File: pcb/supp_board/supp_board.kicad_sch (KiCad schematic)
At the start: 19 parts, among them J1 Conn_01x03_Pin, J2 Conn_01x02_Pin, J3 Screw_Terminal_01x04, J4 Screw_Terminal_01x04, J5 Screw_Terminal_01x04, J6 Conn_01x08_Socket, J7 Conn_01x08_Socket, J8 Conn_01x08_Socket, J9 Conn_01x08_Socket, Q1 IRLZ44N, Q2 IRLZ44N, Q3 IRLZ44N, Q7 IRLZ44N, Q8 IRLZ44N, Q9 IRLZ44N

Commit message: Add work from 2025-07-24 to 2025-07-26
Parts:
- removed J1: Conn_01x03_Pin, Connector_Wire:SolderWire-0.5sqmm_1x03_P4.6mm_D0.9mm_OD2.1mm, symbol Connector:Conn_01x03_Pin
- added C1, C2, C3: C_Polarized, Capacitor_THT:CP_Radial_D8.0mm_P3.50mm, symbol Device:C_Polarized
- added J10: Screw_Terminal_01x03, TerminalBlock:TerminalBlock_MaiXu_MX126-5.0-03P_1x03_P5.00mm, symbol Connector:Screw_Terminal_01x03
- J6, J7, J8, J9: footprint Connector_JST:JST_PH_S8B-PH-K_1x08_P2.00mm_Horizontal -> Connector_JST:JST_PH_B8B-PH-K_1x08_P2.00mm_Vertical
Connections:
- net TX: now reaches A2.1 (GPIO0), J2.2 (Pin_2)
- net GND: now reaches A1.1 (GND), A1.7 (GND), A2.13 (GND), A2.18 (GND), A2.23 (GND), A2.28 (GND), A2.3 (GND), A2.38 (GND), A2.8 (GND), A3.1 (GND), A3.7 (GND), A4.1 (GND), A4.7 (GND), J6.4 (Pin_4), J7.4 (Pin_4), J8.4 (Pin_4)
- net GND: now also C1.2, C2.2, C3.2, J10.2 (Pin_2); no longer J9.2 (Pin_2)
- net RX: now reaches A2.2 (GPIO1), J2.1 (Pin_1)
- net +5V: now reaches A1.10 (M0), A1.11 (M1), A1.12 (M2), A1.13 (~{RST}), A1.14 (~{SLP}), A2.40 (VBUS), A4.10 (M0), A4.11 (M1), A4.12 (M2), A4.13 (~{RST}), A4.14 (~{SLP}), Q7.3 (S), Q8.3 (S), Q9.3 (S)
- net +5V: now also A3.10 (M0), A3.11 (M1), A3.12 (M2), A3.13 (~{RST}), A3.14 (~{SLP}), J10.1 (Pin_1)
- net TPLG_TX: now reaches A2.6 (GPIO4), J6.5 (Pin_5)
- net TPLG_RX: now reaches A2.7 (GPIO5), J6.6 (Pin_6)
- net +24V: now reaches Q1.3 (S), Q2.3 (S), Q3.3 (S)
- net +24V: now also A1.8 (VMOT), A3.8 (VMOT), A4.8 (VMOT), C1.1, C2.1, C3.1, J10.3 (Pin_3)
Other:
- note added: "place @ drv 1"
- note added: "place @ drv 2"
- note added: "place @ drv 3"

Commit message: Add work from 2025-07-27
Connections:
- net GND: now also J9.2 (Pin_2)
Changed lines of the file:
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@@
+	)
+	(symbol
+		(lib_id "power:GND")
+		(at 162.56 123.19 0)
+		(mirror x)
+		(unit 1)
+		(exclude_from_sim no)
+		(in_bom yes)
+		(on_board yes)
+		(dnp no)
+		(property "Reference" "#PWR012"
+			(at 162.56 116.84 0)
+			(effects
+				(font
+					(size 1.27 1.27)
+				)
+				(hide yes)
+			)
+		)
+		(property "Value" "GND"
+			(at 162.56 118.11 0)
+			(effects
+				(font
+					(size 1.27 1.27)
+				)
+			)
+		)
+		(property "Footprint" ""
+			(at 162.56 123.19 0)
+			(effects
+				(font
+					(size 1.27 1.27)
+				)
+				(hide yes)
+			)
+		)
+		(property "Datasheet" ""
+			(at 162.56 123.19 0)
+			(effects
+				(font
+					(size 1.27 1.27)
+				)
+				(hide yes)
+			)
+		)
+		(property "Description" "Power symbol creates a global label with name \"GND\" , ground"
+			(at 162.56 123.19 0)
+			(effects
+				(font
+					(size 1.27 1.27)
+				)
+				(hide yes)
+			)
+		)
+		(pin "1"
+		)
+		(instances
+			(project ""
+				(path "/21a5de1d-7745-4c12-9064-9c9b9fdd4bd4"
+					(reference "#PWR012")
+					(unit 1)
+				)
+			)
+		)
 	)
 	(symbol

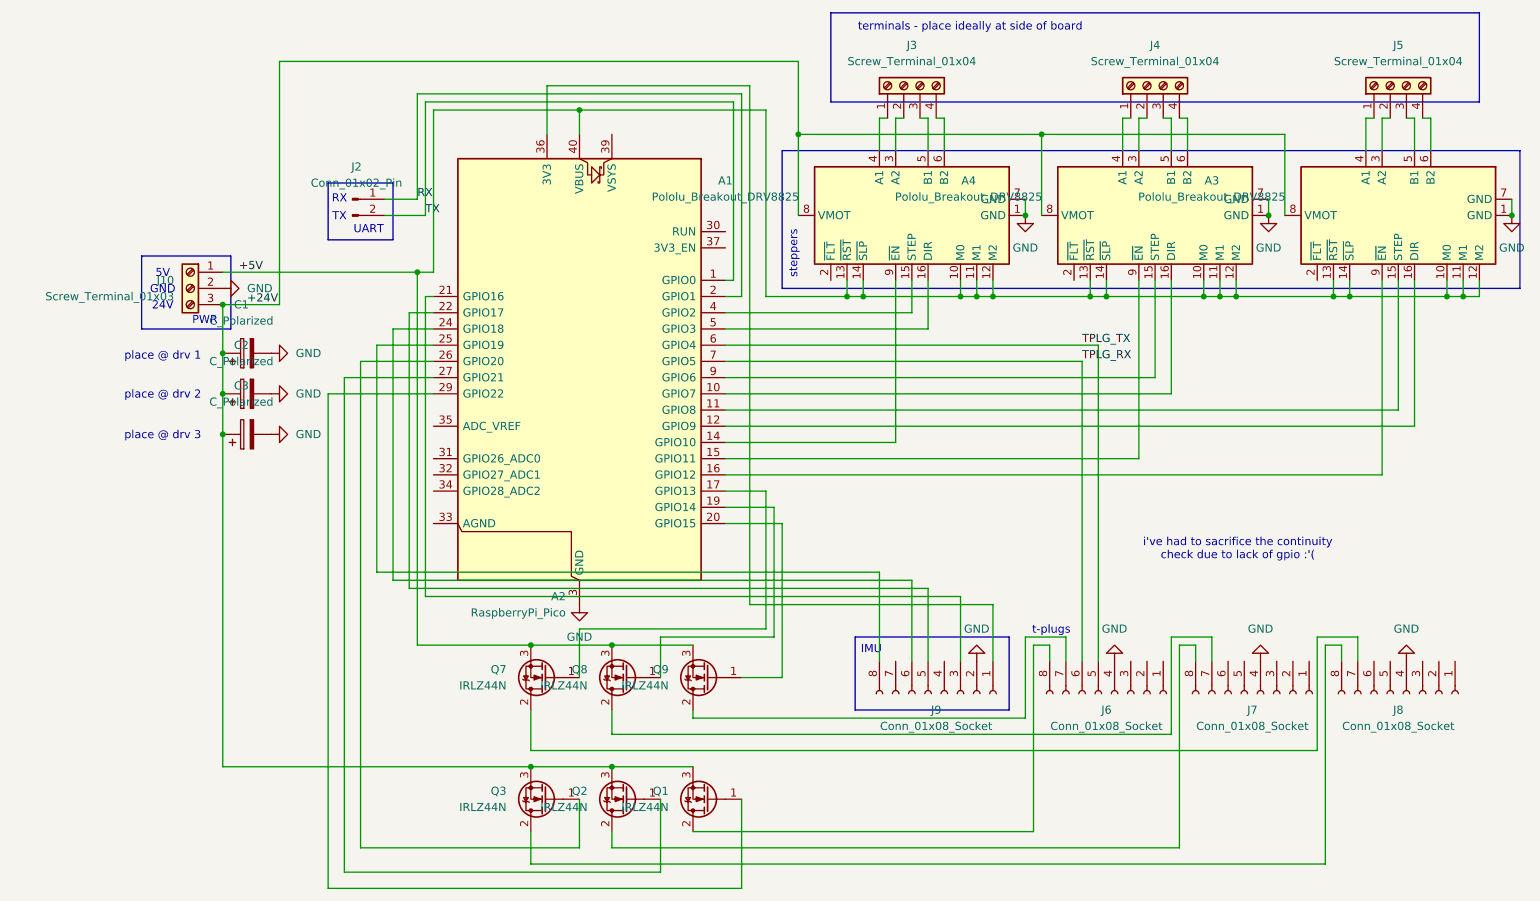
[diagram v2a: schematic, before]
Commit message: Reroute supp. board
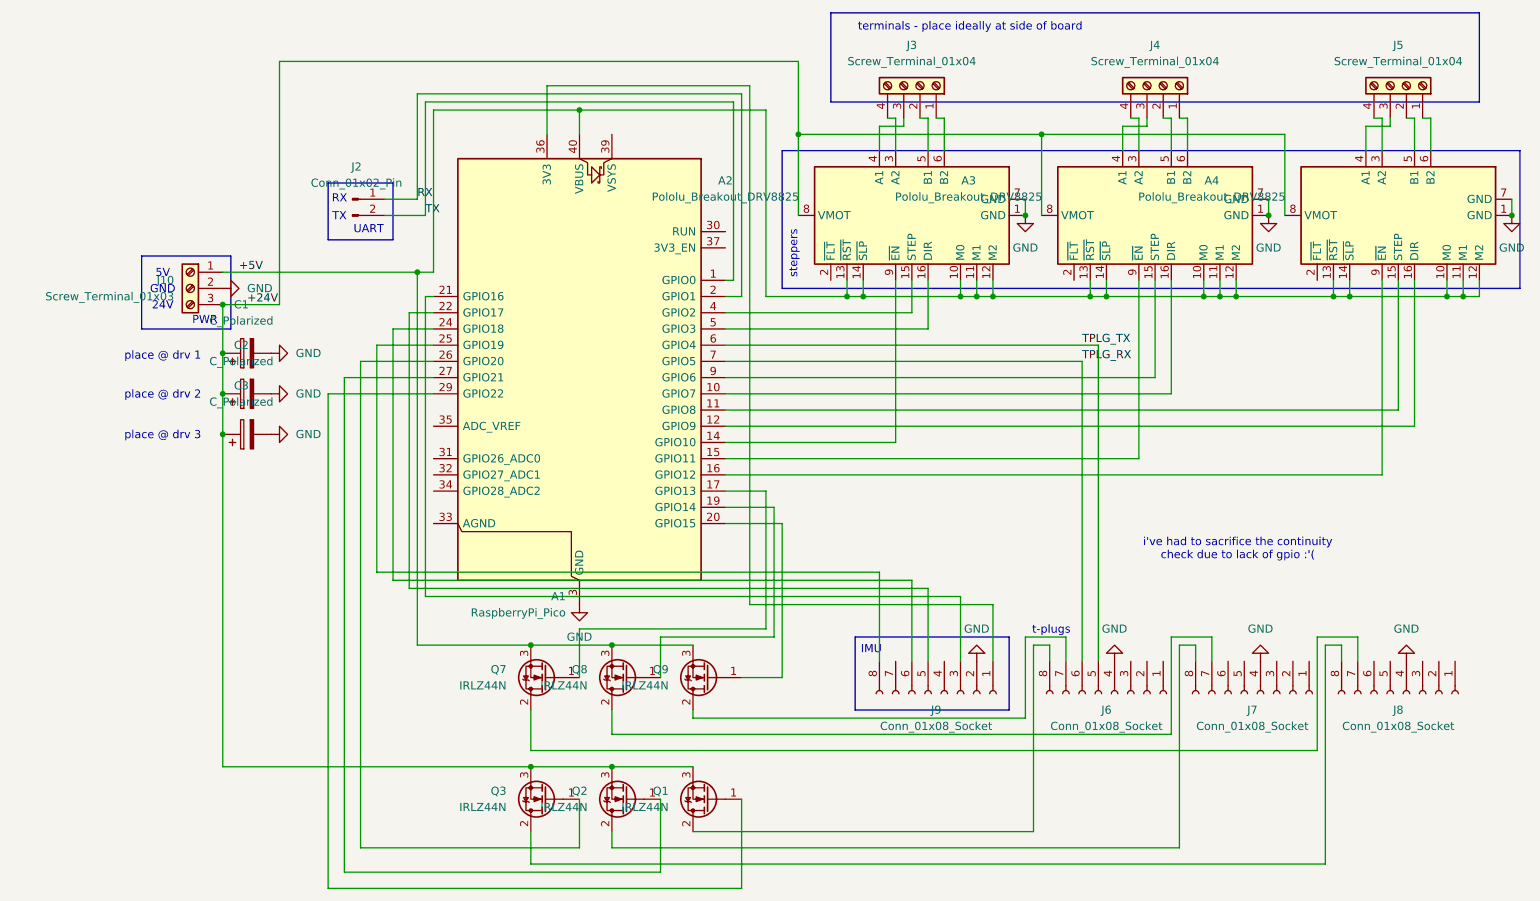
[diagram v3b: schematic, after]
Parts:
- renumbered A2 to A1, A1 to A2, A4 to A3, A3 to A4
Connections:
- net at J4.1 (Pin_1): now also A3.6 (B2); no longer A3.4 (A1)
- net at J4.2 (Pin_2): now also A3.5 (B1); no longer A3.3 (A2)
- net at J4.3 (Pin_3): now also A3.4 (A1); no longer A3.5 (B1)
- net at J4.4 (Pin_4): now also A3.3 (A2); no longer A3.6 (B2)
- net at A2.3 (A2): now also J3.4 (Pin_4); no longer J3.2 (Pin_2)
- net at A2.4 (A1): now also J3.3 (Pin_3); no longer J3.1 (Pin_1)
- net at A2.5 (B1): now also J3.2 (Pin_2); no longer J3.3 (Pin_3)
- net at A2.6 (B2): now also J3.1 (Pin_1); no longer J3.4 (Pin_4)
- net at J5.1 (Pin_1): now also A4.6 (B2); no longer A4.4 (A1)
- net at J5.2 (Pin_2): now also A4.5 (B1); no longer A4.3 (A2)
- net at J5.3 (Pin_3): now also A4.4 (A1); no longer A4.5 (B1)
- net at J5.4 (Pin_4): now also A4.3 (A2); no longer A4.6 (B2)
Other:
- moved on the sheet: J3, J4, J5
